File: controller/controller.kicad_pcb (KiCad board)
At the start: 2 copper layers, 4 parts, among them J1 Conn_01x02_Socket, J2 Conn_01x02_Socket, SW1 SW_Push_Dual, U1 Pico

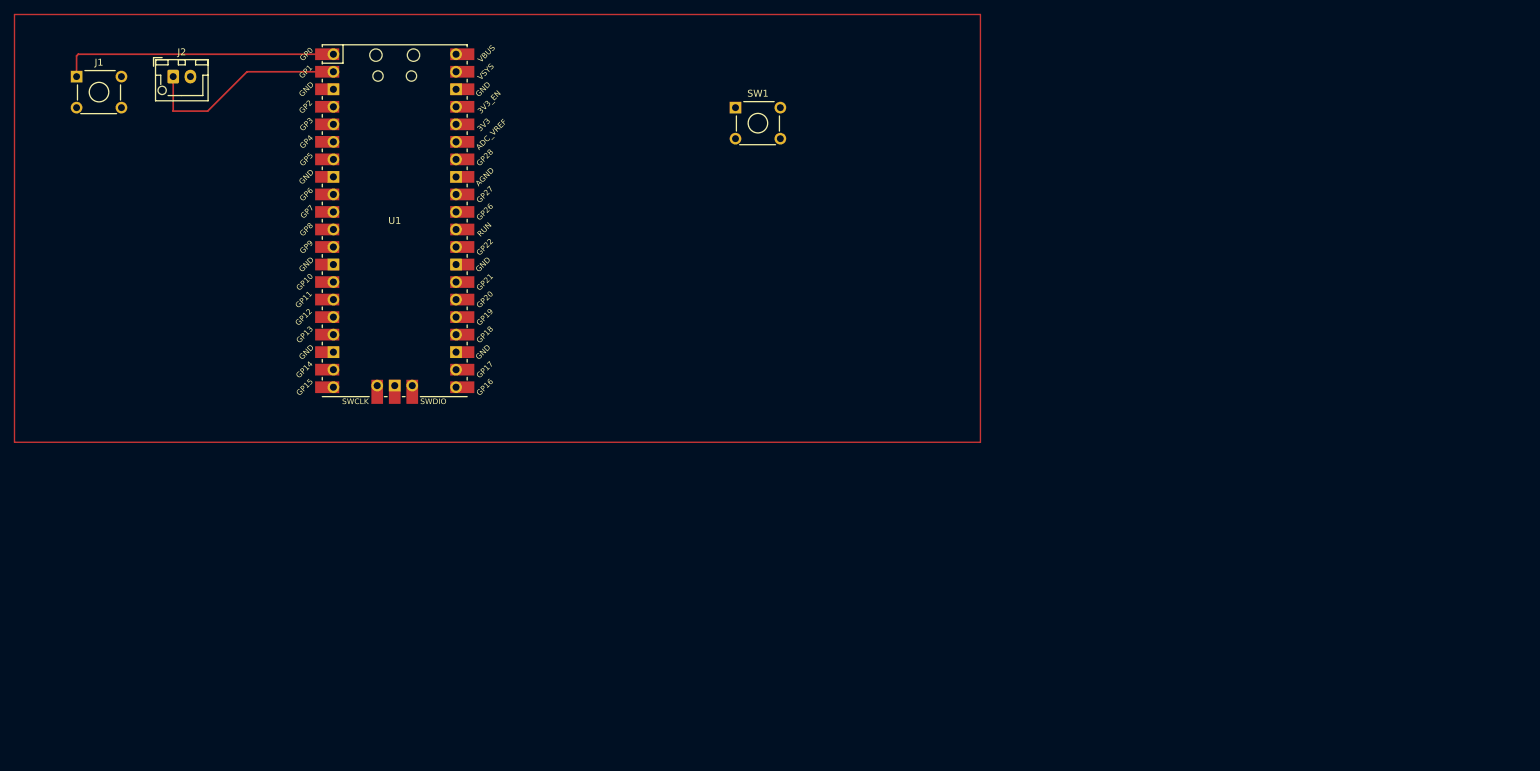
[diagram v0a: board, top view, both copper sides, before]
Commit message: Splitting dpad out into its own board
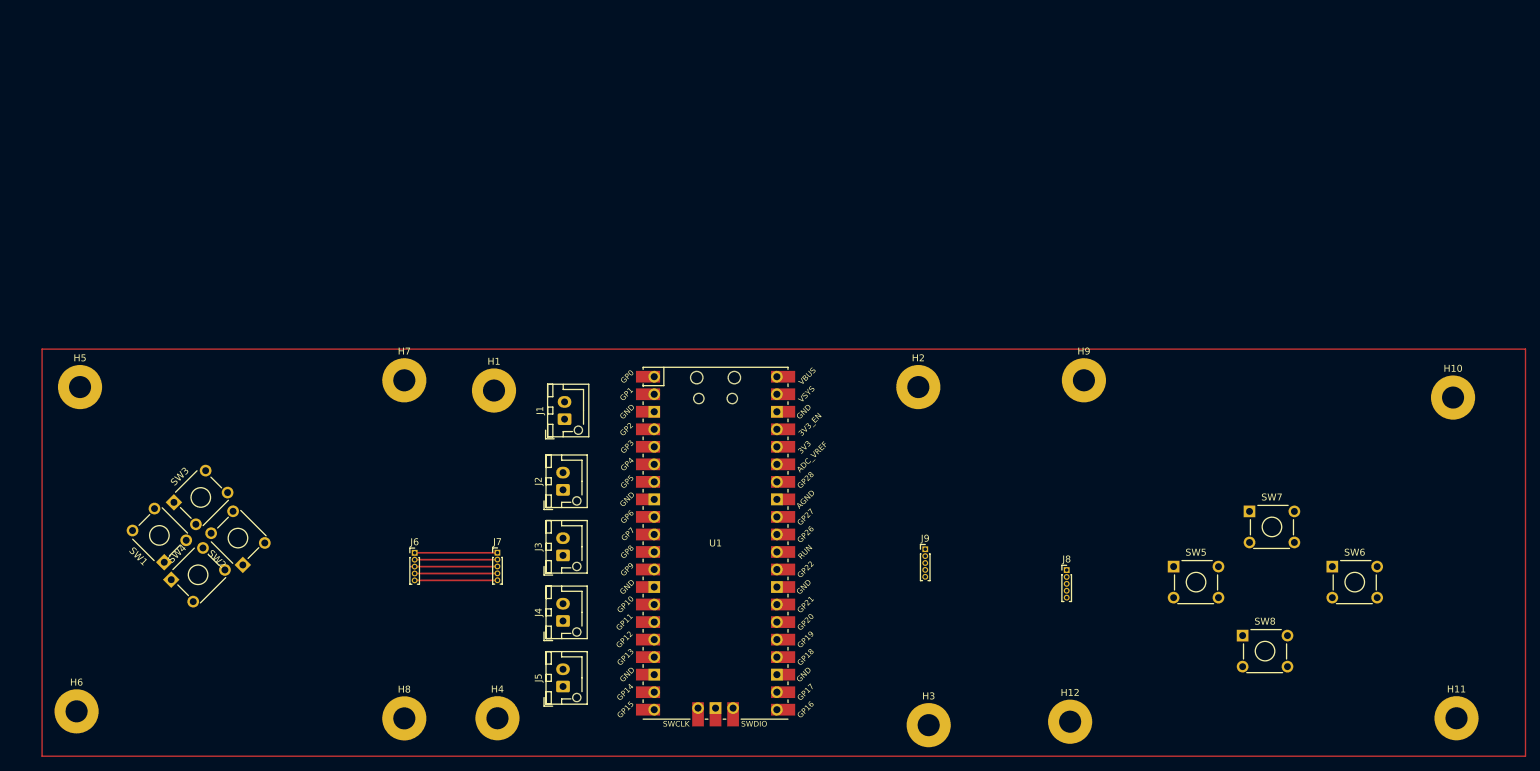
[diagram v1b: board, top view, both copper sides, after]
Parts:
- added H1: MountingHole_Pad, MountingHole:MountingHole_3.2mm_M3_Pad, F.Cu at (111.5, 73.5)
- added H10: MountingHole_Pad, MountingHole:MountingHole_3.2mm_M3_Pad, F.Cu at (250.5, 74.5)
- added H11: MountingHole_Pad, MountingHole:MountingHole_3.2mm_M3_Pad, F.Cu at (251.0, 121.0)
- added H12: MountingHole_Pad, MountingHole:MountingHole_3.2mm_M3_Pad, F.Cu at (195.0, 121.5)
- added H2: MountingHole_Pad, MountingHole:MountingHole_3.2mm_M3_Pad, F.Cu at (173.0, 73.0)
- added H3: MountingHole_Pad, MountingHole:MountingHole_3.2mm_M3_Pad, F.Cu at (174.5, 122.0)
- added H4: MountingHole_Pad, MountingHole:MountingHole_3.2mm_M3_Pad, F.Cu at (112.0, 121.0)
- added H5: MountingHole_Pad, MountingHole:MountingHole_3.2mm_M3_Pad, F.Cu at (51.5, 73.0)
- added H6: MountingHole_Pad, MountingHole:MountingHole_3.2mm_M3_Pad, F.Cu at (51.0, 120.0)
- added H7: MountingHole_Pad, MountingHole:MountingHole_3.2mm_M3_Pad, F.Cu at (98.5, 72.0)
- added H8: MountingHole_Pad, MountingHole:MountingHole_3.2mm_M3_Pad, F.Cu at (98.5, 121.0)
- added H9: MountingHole_Pad, MountingHole:MountingHole_3.2mm_M3_Pad, F.Cu at (197.0, 72.0)
- added J3: Conn_01x02_Socket, Connector_JST:JST_XH_B2B-XH-AM_1x02_P2.50mm_Vertical, F.Cu at (121.5, 97.4)
- added J4: Conn_01x02_Socket, Connector_JST:JST_XH_B2B-XH-AM_1x02_P2.50mm_Vertical, F.Cu at (121.5, 106.9)
- added J5: Conn_01x02_Socket, Connector_JST:JST_XH_B2B-XH-AM_1x02_P2.50mm_Vertical, F.Cu at (121.5, 116.4)
- added J6: Conn_01x05_Socket, Connector_PinHeader_1.00mm:PinHeader_1x05_P1.00mm_Vertical, F.Cu at (100.0, 97.0)
- added J7: Conn_01x05_Socket, Connector_PinHeader_1.00mm:PinHeader_1x05_P1.00mm_Vertical, F.Cu at (112.0, 97.0)
- added J8: Conn_01x05_Socket, Connector_PinHeader_1.00mm:PinHeader_1x05_P1.00mm_Vertical, F.Cu at (194.5, 99.5)
- added J9: Conn_01x05_Socket, Connector_PinHeader_1.00mm:PinHeader_1x05_P1.00mm_Vertical, F.Cu at (174.0, 96.5)
- added SW2: SW_Push_Dual, Button_Switch_THT:SW_TH_Tactile_Omron_B3F-10xx, F.Cu at (75.1, 98.8)
- added SW3: SW_Push_Dual, Button_Switch_THT:SW_TH_Tactile_Omron_B3F-10xx, F.Cu at (65.1, 89.7)
- added SW4: SW_Push_Dual, Button_Switch_THT:SW_TH_Tactile_Omron_B3F-10xx, F.Cu at (64.7, 100.9)
- added SW5: SW_Push_Dual, Button_Switch_THT:SW_TH_Tactile_Omron_B3F-10xx, F.Cu at (210.0, 99.0)
- added SW6: SW_Push_Dual, Button_Switch_THT:SW_TH_Tactile_Omron_B3F-10xx, F.Cu at (233.0, 99.0)
- added SW7: SW_Push_Dual, Button_Switch_THT:SW_TH_Tactile_Omron_B3F-10xx, F.Cu at (221.0, 91.0)
- added SW8: SW_Push_Dual, Button_Switch_THT:SW_TH_Tactile_Omron_B3F-10xx, F.Cu at (220.0, 109.0)
- J1: footprint Button_Switch_THT:SW_TH_Tactile_Omron_B3F-10xx -> Connector_JST:JST_XH_B2B-XH-AM_1x02_P2.50mm_Vertical
- moved SW1 105.8 mm to (63.7, 98.4), turned to 135 degrees
- moved J1 86.4 mm to (121.7, 77.7), turned to 90 degrees
- moved J2 82.3 mm to (121.5, 87.9), turned to 90 degrees
- moved U1 65.9 mm to (143.6, 95.6)
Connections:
- U1 pad 1: B1 -> I2C SDL
- U1 pad 14: unconnected-(U1-GPIO10-Pad14) -> D1
- U1 pad 15: unconnected-(U1-GPIO11-Pad15) -> D2
- U1 pad 16: unconnected-(U1-GPIO12-Pad16) -> D3
- U1 pad 17: unconnected-(U1-GPIO13-Pad17) -> D4
- U1 pad 2: B2 -> I2C SDA
- U1 pad 24: unconnected-(U1-GPIO18-Pad24) -> D8
- U1 pad 25: unconnected-(U1-GPIO19-Pad25) -> D7
- U1 pad 26: unconnected-(U1-GPIO20-Pad26) -> D6
- U1 pad 27: D1 -> D5
- U1 pad 4: unconnected-(U1-GPIO2-Pad4) -> B1
- U1 pad 42: GND -> unconnected-(U1-GND-Pad42)
- U1 pad 5: unconnected-(U1-GPIO3-Pad5) -> B2
- U1 pad 6: unconnected-(U1-GPIO4-Pad6) -> B3
- U1 pad 7: unconnected-(U1-GPIO5-Pad7) -> B4
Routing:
- net B1: track 40.3 -> 0.00 mm
- net B2: track 30.6 -> 0.00 mm
- net D3: track 0.00 -> 12.6 mm
- net D4: track 0.00 -> 12.1 mm
- net GND: track 0.00 -> 12.0 mm
- net D2: track 0.00 -> 12.0 mm
- net D1: track 0.00 -> 12.0 mm
